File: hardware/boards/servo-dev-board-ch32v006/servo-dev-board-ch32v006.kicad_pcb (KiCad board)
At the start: 4 copper layers, 60 x 60 mm, 88 parts, among them J1 JST-PH-H, J2 TERM, J3 PIN-V, J4 JST-ZH-H, J5 PIN-V, J6 PIN-V, J7 PIN-V, J8 PIN-V, J9 JST-PH-V, SW1 SW_Push, U1 HT7533-1, U2 DRV8212PDSGR, U3 CH32V006F8P6, U4 74LVC2G241

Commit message: update board
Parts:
- added JP1: Jumper_2_Open, Connector_PinHeader_2.54mm:PinHeader_1x02_P2.54mm_Vertical, F.Cu at (172.3, 81.9)
- moved R14 5.33 mm to (169.5, 79.4), turned to -90 degrees
- moved R16 2.62 mm to (175.1, 79.4), turned to -90 degrees
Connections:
- J1 pad 1: VBAT -> GND
- J1 pad 2: GND -> VBAT
- U3 pad 1: /VPOS -> /ENCA
- U3 pad 20: /ENCA -> /VPOS
- U4 pad 6: /RX -> /COMMS/JP_RX
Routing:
- net /MCU/nRST: track 71.6 -> 4.74 mm, vias 2 -> 0
- net /VNTC: track 64.8 -> 43.7 mm
- net /ENCA: track 49.6 -> 57.4 mm, vias 1 -> 2
- net /MCU/SWDIO: track 15.5 -> 21.4 mm
- net /COMMS/JP_RX: track 0.00 -> 5.21 mm
- net /EN: track 70.2 -> 74.1 mm
- net /DBG: track 50.8 -> 54.3 mm
- net /VPOS: track 63.8 -> 60.5 mm, vias 2 -> 3
- net /IN2: track 49.3 -> 52.4 mm
- net /RX: track 71.7 -> 70.2 mm, vias 2 -> 3
- net /STAT: track 51.0 -> 52.2 mm
- net /ENCB: track 46.5 -> 47.5 mm
- net /IN1: track 53.7 -> 52.9 mm
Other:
- board text added: "QA"
- board text added: "QB"

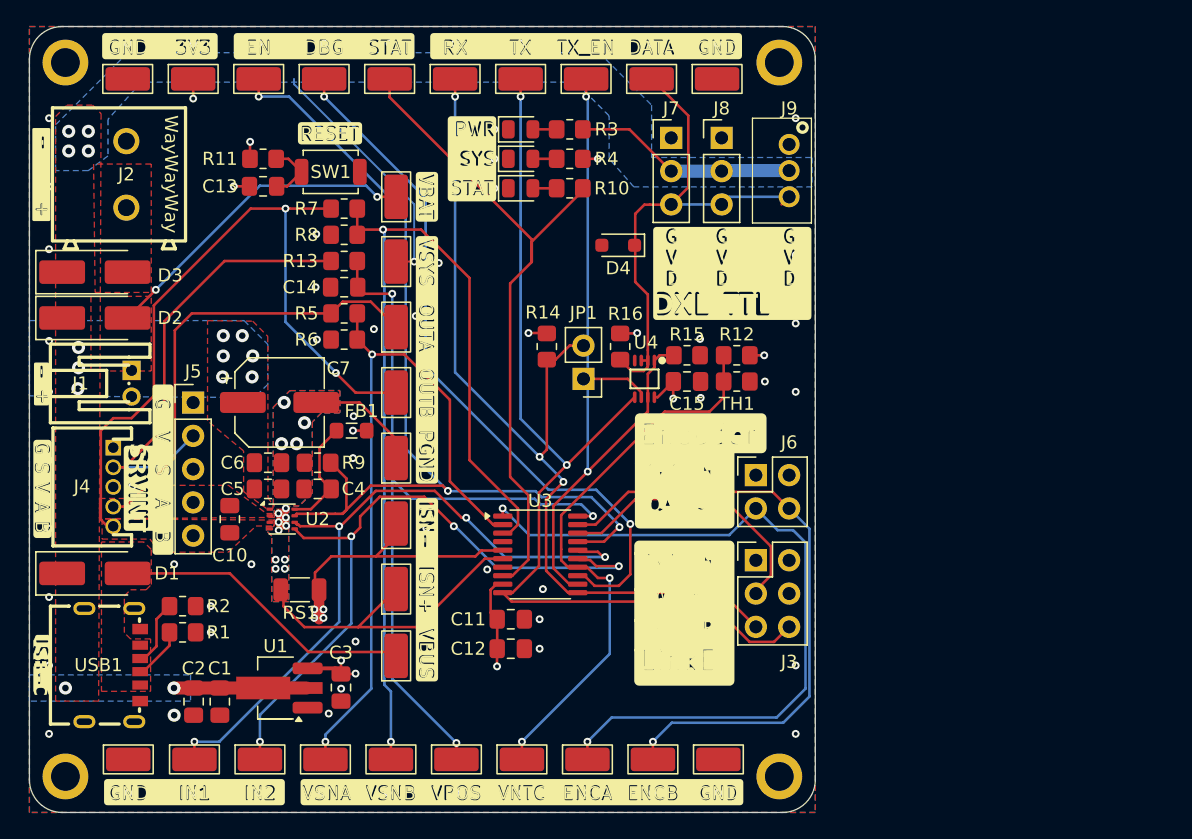
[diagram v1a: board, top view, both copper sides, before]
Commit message: updated schematics. ERC on schematics is now passing
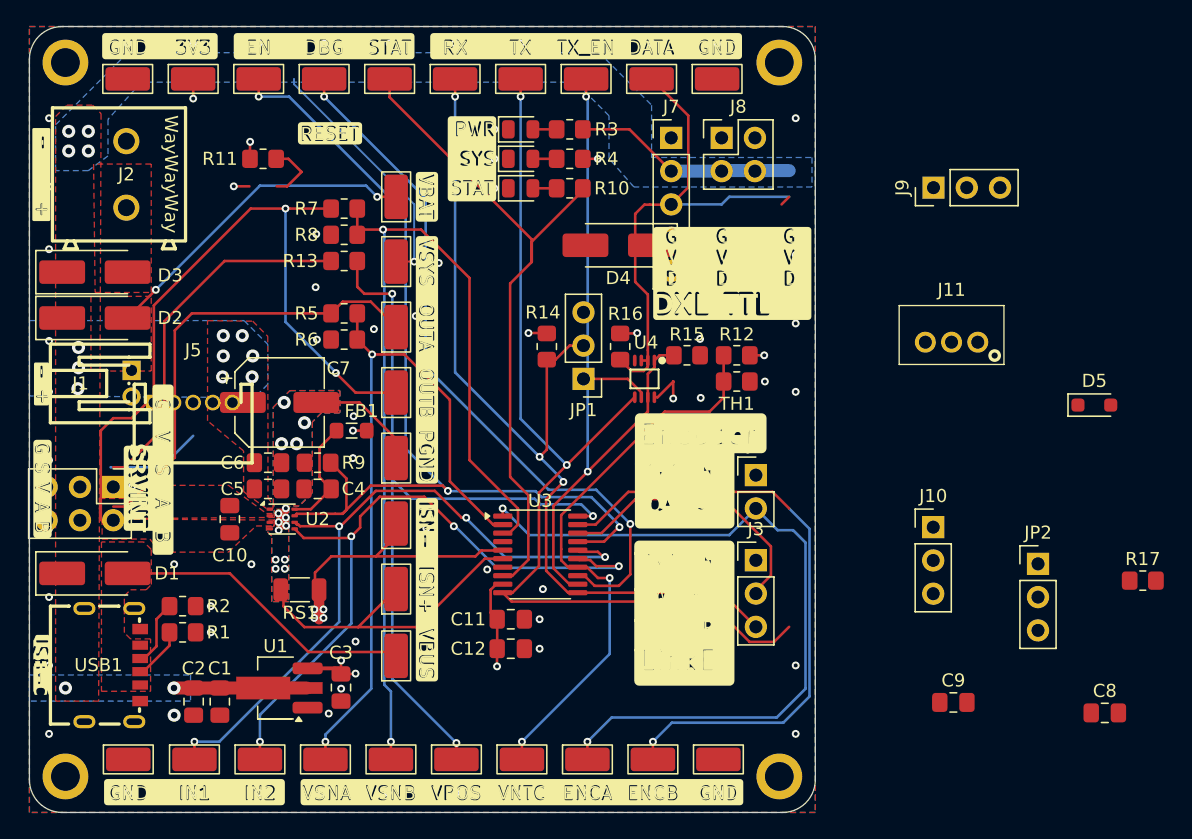
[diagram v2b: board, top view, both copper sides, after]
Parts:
- removed C13, C14, C15: 0.1µF, Capacitor_SMD:C_0805_2012Metric_Pad1.18x1.45mm_HandSolder
- removed SW1: SW_Push, Button_Switch_SMD:SW_SPST_TS-1088-xR020
- added C8: 0.1µF, Capacitor_SMD:C_0805_2012Metric_Pad1.18x1.45mm_HandSolder, F.Cu at (212.1, 107.4)
- added C9: 10µF, Capacitor_SMD:C_0805_2012Metric_Pad1.18x1.45mm_HandSolder, F.Cu at (200.5, 106.6)
- added D5: PESD5V0L1BA, Diode_SMD:D_SOD-323_HandSoldering, F.Cu at (211.3, 83.9)
- added J10: PIN-V, Connector_PinHeader_2.54mm:PinHeader_1x03_P2.54mm_Vertical, F.Cu at (199.0, 93.2)
- added J11: JST-PH-V, shared:CONN-TH_B3B-PH-K-S, F.Cu at (200.4, 79.1)
- added JP2: TLL | UART, Connector_PinHeader_2.54mm:PinHeader_1x03_P2.54mm_Vertical, F.Cu at (207.0, 96.0)
- added R17: 10kΩ, Resistor_SMD:R_0805_2012Metric_Pad1.20x1.40mm_HandSolder, F.Cu at (215.0, 97.3)
- C11: value 10µF -> 0.1µF
- D4: value PESD5V0L1BA -> SS54; footprint Diode_SMD:D_SOD-323_HandSoldering -> Diode_SMD:D_SMA_Handsoldering
- J3: value PIN-V -> Conn_01x03; footprint Connector_PinHeader_2.54mm:PinHeader_2x03_P2.54mm_Vertical -> Connector_PinHeader_2.54mm:PinHeader_1x03_P2.54mm_Vertical
- J4: value JST-ZH-H -> PIN-V; footprint shared:CONN-TH_S5B-ZR-LF-SN -> Connector_PinHeader_2.54mm:PinHeader_2x03_P2.54mm_Vertical
- J5: value PIN-V -> JST-ZH-H; footprint Connector_PinHeader_2.54mm:PinHeader_1x05_P2.54mm_Vertical -> shared:CONN-TH_S5B-ZR-LF-SN
- J6: value PIN-V -> NTC EXT; footprint Connector_PinHeader_2.54mm:PinHeader_2x02_P2.54mm_Vertical -> Connector_PinHeader_2.54mm:PinHeader_1x02_P2.54mm_Vertical
- J7: footprint Connector_PinHeader_2.54mm:PinHeader_1x03_P2.54mm_Vertical -> Connector_PinHeader_2.54mm:PinHeader_1x05_P2.54mm_Vertical
- J8: footprint Connector_PinHeader_2.54mm:PinHeader_1x03_P2.54mm_Vertical -> Connector_PinHeader_2.54mm:PinHeader_2x02_P2.54mm_Vertical
- J9: value JST-PH-V -> PIN-V; footprint shared:CONN-TH_B3B-PH-K-S -> Connector_PinHeader_2.54mm:PinHeader_1x03_P2.54mm_Vertical
- JP1: value Jumper_2_Open -> NTC|NTC_EXT; footprint Connector_PinHeader_2.54mm:PinHeader_1x02_P2.54mm_Vertical -> Connector_PinHeader_2.54mm:PinHeader_1x03_P2.54mm_Vertical
- R10: value 1kΩ -> 10kΩ
- R12: value 10kΩ -> 1kΩ
- R13: value 4.7kΩ -> 10kΩ
- R14: value 10kΩ -> 4.7kΩ
- R9: value 10kΩ -> 20kΩ
- moved J9 11.1 mm to (199.0, 67.3)
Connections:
- C10 pad 1: /MOT_A -> +3V3
- C10 pad 2: /MOT_B -> GND
- C11 pad 1: +3V3 -> /VPOS
- D4 pad 1: /DATA -> VSYS
- D4 pad 2: GND -> VPROG
- J3 pad 1: +3V3 -> VSYS
- J3 pad 2: GND -> /IN1
- J3 pad 3: /MCU/SWDIO -> GND
- J4 pad 1: GND -> +3V3
- J4 pad 2: /SERVO_IO/POT -> GND
- J4 pad 3: +3V3 -> /MCU/SWDIO
- J4 pad 4: /MOT_A -> VPROG
- J4 pad 5: /MOT_B -> /RX
- J6 pad 1: +3V3 -> Net-(J6-Pin_1)
- J7 pad 2: VSYS -> /SERVO_IO/POT
- J7 pad 3: /DATA -> +3V3
- J8 pad 1: GND -> +3V3
- J8 pad 2: VSYS -> GND
- J8 pad 3: /DATA -> /ENCA
- JP1 pad 1: /COMMS/JP_RX -> Net-(J6-Pin_1)
- JP1 pad 2: /RX -> /VNTC
- R10 pad 1: /STAT -> /VSNS
- R10 pad 2: Net-(LED3-A) -> GND
- R11 pad 1: +3V3 -> /EN
- R11 pad 2: /MCU/nRST -> PGND
- R12 pad 1: +3V3 -> /STAT
- R12 pad 2: /VNTC -> Net-(LED3-A)
- R13 pad 1: /VPOS -> +3V3
- R13 pad 2: /SERVO_IO/POT -> /VNTC
- R14 pad 1: +3V3 -> /VPOS
- R14 pad 2: /RX -> /SERVO_IO/POT
- R15 pad 1: /TX_EN -> +3V3
- R15 pad 2: GND -> /RX
- R16 pad 1: +3V3 -> /TX_EN
- R16 pad 2: /DATA -> GND
- R9 pad 1: /EN -> VSYS
- R9 pad 2: PGND -> /VSNS
- TH1 pad 1: /VNTC -> Net-(JP1-B)
- U3 pad 1: /ENCA -> /ENCB
- U3 pad 13: /DBG -> /EN
- U3 pad 17: /EN -> /STAT
- U3 pad 19: /ENCB -> /VPOS
- U3 pad 20: /VPOS -> /ENCA
- U3 pad 4: /MCU/nRST -> /ISNS-
- U3 pad 5: /ISNS- -> /VSNS
- U3 pad 8: /STAT -> /DBG
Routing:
- net /VNTC: track 43.7 -> 71.6 mm
- net /SERVO_IO/POT: track 35.2 -> 7.29 mm
- net /VPOS: track 60.5 -> 79.6 mm
- net /ENCB: track 47.5 -> 29.8 mm
- net +3V3: track 23.5 -> 18.4 mm, vias 11 -> 10
- net /MCU/nRST: track 4.74 -> 0.00 mm
- net PGND: track 8.70 -> 13.4 mm
- net /TX_EN: track 53.1 -> 54.4 mm
- net /EN: track 74.1 -> 75.4 mm
- net /STAT: track 52.2 -> 53.3 mm, vias 0 -> 1

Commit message: completed routing.
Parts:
- J3: value Conn_01x03 -> SERVO
- moved C8 68.4 mm to (145.3, 92.5), turned to -90 degrees
- moved J4 49.4 mm to (185.5, 95.8), turned to 0 degrees
- moved J3 49.1 mm to (144.5, 68.7), turned to 180 degrees
- moved JP2 46.4 mm to (166.2, 73.9), turned to 90 degrees
- moved R17 46.3 mm to (175.2, 73.7)
- moved J7 41.7 mm to (142.5, 83.7)
- moved D5 38.0 mm to (175.3, 71.7), turned to 180 degrees
- moved D4 36.9 mm to (185.2, 107.2), turned to 0 degrees
- moved J10 34.9 mm to (182.8, 62.3)
- moved C9 34.4 mm to (166.8, 100.2)
- moved C11 28.4 mm to (154.0, 74.9), turned to 180 degrees
- moved J8 25.9 mm to (185.5, 89.2)
- moved C12 24.1 mm to (173.2, 79.3)
- moved C10 23.6 mm to (166.8, 102.5), turned to 0 degrees
- moved R11 23.6 mm to (152.0, 88.3), turned to 180 degrees
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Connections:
- net Net-(J6-Pin_1) renamed /SERVO_IO/VNTC_EXT
- net Net-(JP1-B) renamed /SERVO_IO/VNTC_INT
- J3 pad 1: VSYS -> GND
- J3 pad 2: /IN1 -> VSYS
- J3 pad 3: GND -> /IN1
- J4 pad 1: +3V3 -> /RX
- J4 pad 2: GND -> /TX
- J4 pad 3: /MCU/SWDIO -> +3V3
- J4 pad 4: VPROG -> GND
- J4 pad 5: /RX -> /MCU/SWDIO
- J4 pad 6: /TX -> VPROG
- JP2 pad 2: /COMMS/JP_RX -> /RX
- JP2 pad 3: /RX -> /COMMS/JP_RX
- U3 pad 1: /ENCB -> /ENCA
- U3 pad 13: /EN -> /DBG
- U3 pad 20: /ENCA -> /ENCB
- U3 pad 8: /DBG -> /EN
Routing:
- net VSYS: track 46.3 -> 99.7 mm, vias 16 -> 18
- net /VSNS: track 0.00 -> 40.4 mm
- net /IN1: track 52.9 -> 84.5 mm
- net /VNTC: track 71.6 -> 41.5 mm
- net /SERVO_IO/POT: track 7.29 -> 34.3 mm
- net /VPOS: track 79.6 -> 62.1 mm
- net /ENCB: track 29.8 -> 47.2 mm, vias 1 -> 2
- net /EN: track 75.4 -> 64.4 mm, vias 3 -> 4
- net /TX_EN: track 54.4 -> 45.9 mm
- net /TX: track 74.4 -> 66.2 mm
- net /SERVO_IO/VNTC_EXT: track 0.00 -> 8.17 mm
- net /DBG: track 54.3 -> 46.9 mm
- net VPROG: track 0.00 -> 6.92 mm
- net /RX: track 70.2 -> 64.8 mm
- net /MCU/SWDIO: track 21.4 -> 16.6 mm, vias 0 -> 1
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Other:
- board text added: "5V"
- board text added: "EXT"
- board text added: "HDR-2P"
- board text added: "HDR-5P"
- board text added: "INT"
- board text added: "MCU: CH32V006F8P6 DRV: DRV8212PDSGR LDO: HT7533-1 BUF: 74LVC2G241 RS1: 10mOhm ~1% 333mW"
- board text added: "NC"
- board text added: "NTC"
- board text added: "OSC Dev V006 Rev. B Feb. 2026"
- board text added: "PWM"
- board text added: "SCREW TERM"
- board text added: "TTL"
- board text removed: "BRD: servo-dev-board-ch32v006 MCU: CH32V006F8P6 DRV: DRV8212PDSGR LDO: HT7533-1 BUF: 74LVC2G241 RS1: 10mOhm ~1% 333mW REV: B"
- board text removed: "OpenServoCore Dev Board V1 Feb. 2026"
- board text removed: "RESET"
- board text removed: "RST"
- board text removed: "TERM-5.08 2P"

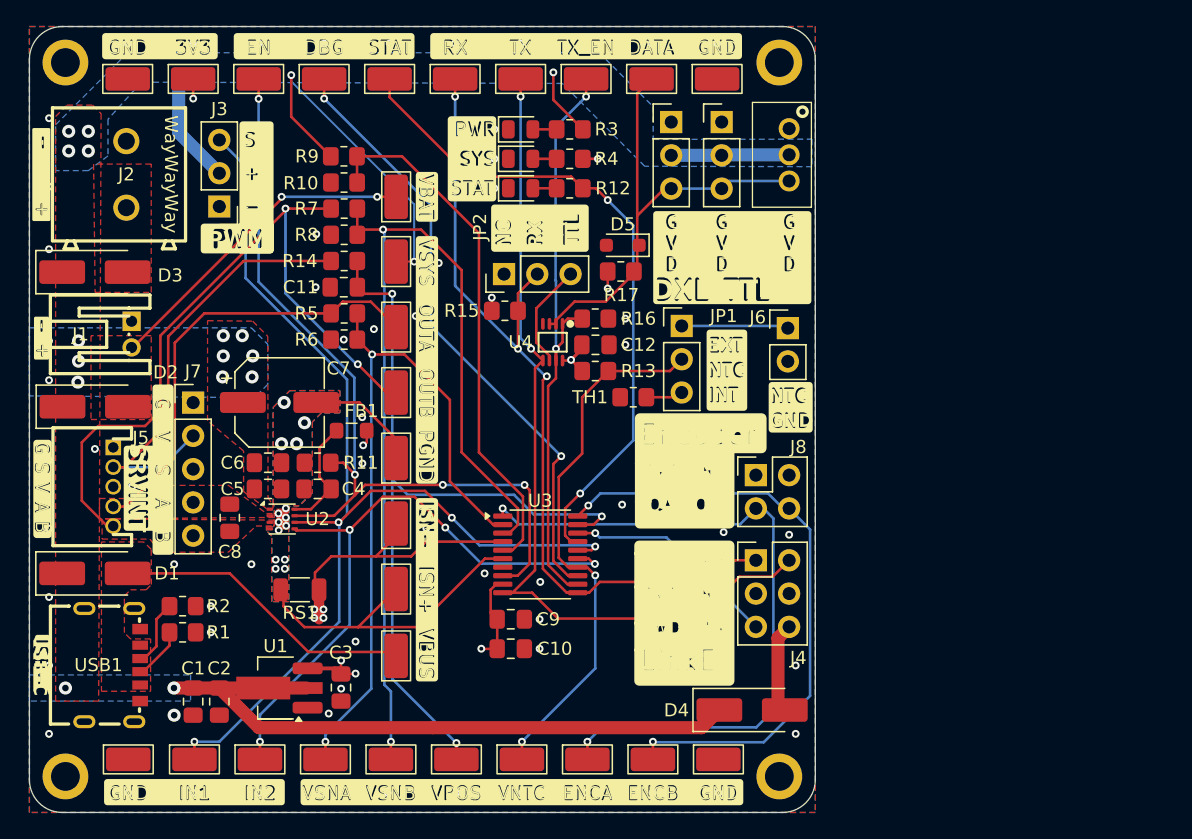
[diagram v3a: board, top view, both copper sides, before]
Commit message: adding ground vias
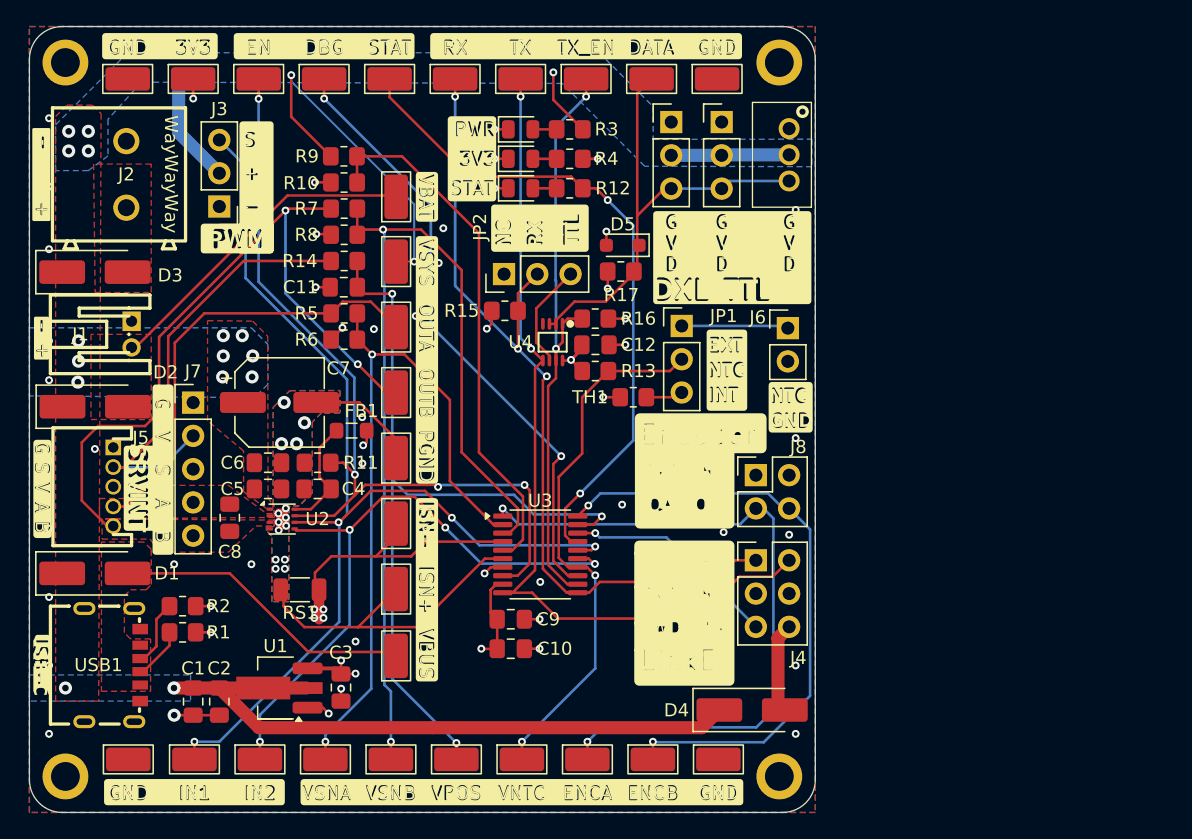
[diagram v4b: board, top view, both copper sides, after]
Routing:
- net GND: track 2.25 -> 27.5 mm, vias 67 -> 74
- net +3V3: track 22.3 -> 22.9 mm
- net VBAT: vias 2 -> 0
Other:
- board text removed: "SYS"

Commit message: update bom and component properties
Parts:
- J10, J9: value PIN-V -> PIN-1-3P
- J3: value SERVO -> PIN-1-3P
- J4: value PIN-V -> PIN-2-3P
- J6: value NTC EXT -> PIN-1-2P
- J7: value PIN-V -> PIN-1-5P
- J8: value PIN-V -> PIN-2-2P
- JP1: value NTC|NTC_EXT -> JP-3
- JP2: value TLL | UART -> JP-3
